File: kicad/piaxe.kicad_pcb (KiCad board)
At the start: 4 copper layers, 85 x 56 mm, 109 parts, among them J1 Barrel_Jack_Switch, J2 Conn_02x20_Odd_Even, J3 Conn_01x05, M1 Fan_4pin, Q1 CSD17576Q5B, Q2 CSD17308Q3, Q5 BSS138, Q6 BSS138, Q9 BSS138, U1 TPS40305, U13 TMP1075, U14 BM1366_mode1, U15 2N7001TDCK, U16 2N7001TDCK, U5 MCP1824T-1802E, U6 MCP1824T-0802E, U7 25MHz

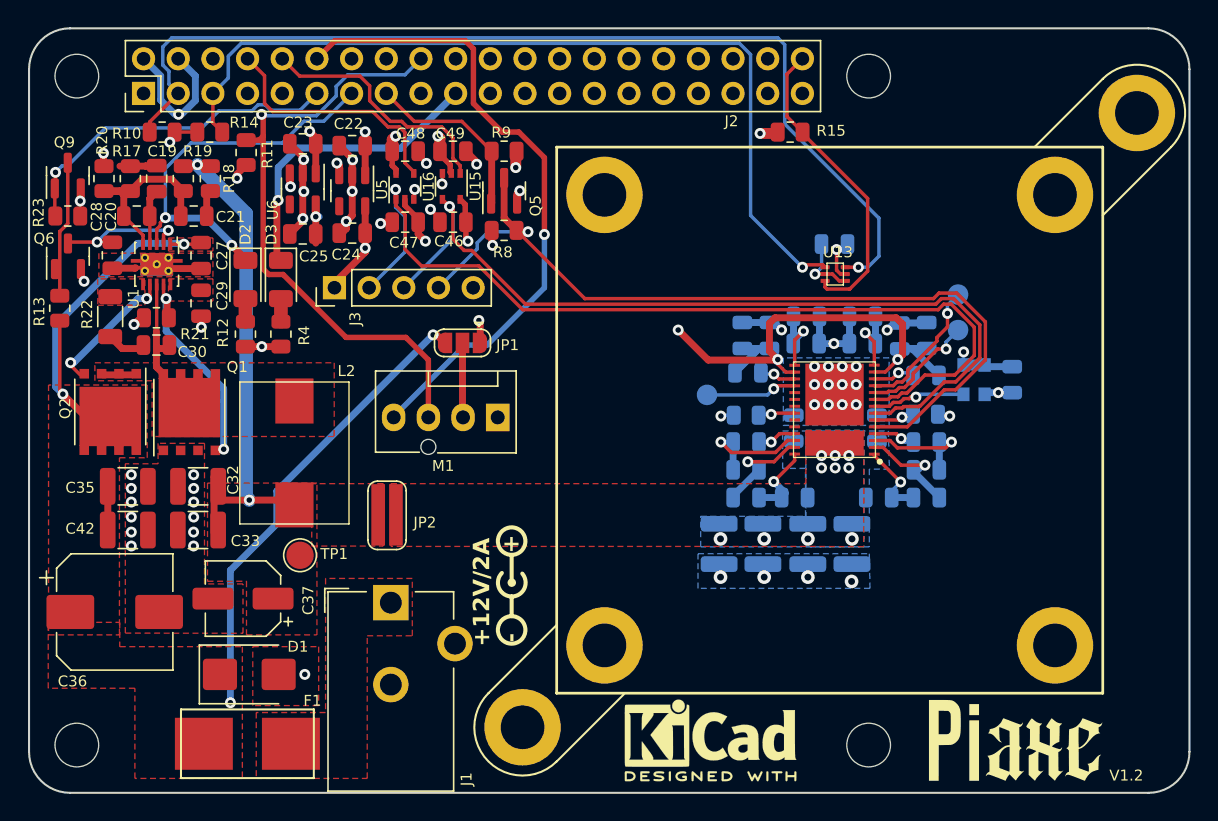
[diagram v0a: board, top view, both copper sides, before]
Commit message: added solderjumper to enable the buck without Pi, changed LED values to 560R
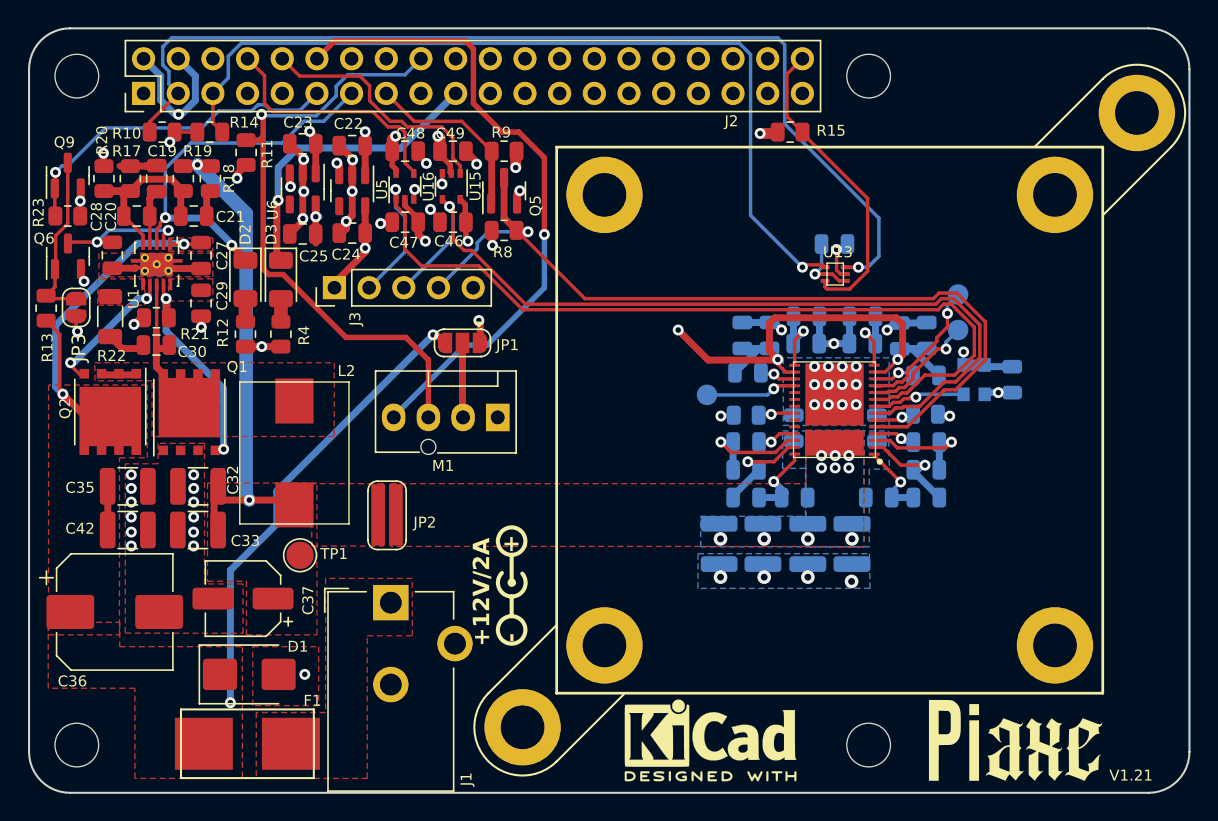
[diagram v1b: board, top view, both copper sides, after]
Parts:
- added JP3: SolderJumper_2_Open, Jumper:SolderJumper-2_P1.3mm_Open_RoundedPad1.0x1.5mm, F.Cu at (176.8, 76.2)
- R12, R4: value 1k -> 560
- moved R13 1.00 mm to (174.6, 76.3)
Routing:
- net Net-(JP3-A): track 10.1 -> 12.8 mm
- net GND: track 114.7 -> 115.9 mm, vias 57 -> 58
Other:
- board text added: "V1.21"
- board text removed: "V1.2"

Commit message: fixed net labeling to 1.2V
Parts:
- TP1: value +1V5 -> +1V2
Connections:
- net +1V5 renamed +1V2
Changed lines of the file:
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@@
   (net 5 "Net-(U14-VDD2_0)")
   (net 6 "Net-(U14-VDD1_0)")
-  (net 7 "+1V5")
+  (net 7 "+1V2")
   (net 8 "Net-(U14-VDD1_1)")
   (net 9 "Net-(U14-VDD2_1)")
@@
       ))
     (pad "2" smd custom (at 0.524 -0.234) (size 1 4.5) (layers "F.Cu" "F.Mask")
-      (net 7 "+1V5") (pinfunction "B") (pintype "passive") (zone_connect 2) (thermal_bridge_angle 45)
+      (net 7 "+1V2") (pinfunction "B") (pintype "passive") (zone_connect 2) (thermal_bridge_angle 45)
       (options (clearance outline) (anchor rect))
       (primitives
@@
         (effects (font (size 0.8 0.8) (thickness 0.15)))
     )
-    (fp_text value "+1V5" (at 0 2.05) (layer "F.Fab")
+    (fp_text value "+1V2" (at 0 2.05) (layer "F.Fab")
         (effects (font (size 1 1) (thickness 0.15)))
     )
@@
       (net 8 "Net-(U14-VDD1_1)") (pinfunction "VDD1_1") (pintype "input") (thermal_bridge_angle 45))
     (pad "29" smd rect locked (at 0 -2.468 180) (size 4.277 1.81) (layers "F.Cu" "F.Mask")
-      (net 7 "+1V5") (pinfunction "VDD") (pintype "input") (thermal_bridge_angle 45))
+      (net 7 "+1V2") (pinfunction "VDD") (pintype "input") (thermal_bridge_angle 45))
     (pad "30" smd rect locked (at 0 1.108 180) (size 4.277 4.53) (layers "F.Cu" "F.Mask")
       (net 1 "GND") (pinfunction "GND") (pintype "input") (thermal_bridge_angle 45))
@@
       (stroke (width 0.1) (type solid)) (layer "B.Fab"))
     (pad "1" smd roundrect (at -0.95 0 90) (size 1 1.45) (layers "B.Cu" "B.Paste" "B.Mask") (roundrect_rratio 0.25)
-      (net 7 "+1V5") (pintype "passive"))
+      (net 7 "+1V2") (pintype "passive"))
     (pad "2" smd roundrect (at 0.95 0 90) (size 1 1.45) (layers "B.Cu" "B.Paste" "B.Mask") (roundrect_rratio 0.25)
       (net 1 "GND") (pintype "passive"))
@@
       (stroke (width 0.1) (type solid)) (layer "B.Fab"))
     (pad "1" smd roundrect (at -0.95 0 90) (size 1 1.45) (layers "B.Cu" "B.Paste" "B.Mask") (roundrect_rratio 0.25)
-      (net 7 "+1V5") (pintype "passive"))
+      (net 7 "+1V2") (pintype "passive"))
     (pad "2" smd roundrect (at 0.95 0 90) (size 1 1.45) (layers "B.Cu" "B.Paste" "B.Mask") (roundrect_rratio 0.25)
       (net 1 "GND") (pintype "passive"))
@@
       (stroke (width 0.1) (type solid)) (layer "B.Fab"))
     (pad "1" smd roundrect (at -1.475 0 270) (size 1.15 2.7) (layers "B.Cu" "B.Paste" "B.Mask") (roundrect_rratio 0.2173913043)
-      (net 7 "+1V5") (pintype "passive"))
+      (net 7 "+1V2") (pintype "passive"))
     (pad "2" smd roundrect (at 1.475 0 270) (size 1.15 2.7) (layers "B.Cu" "B.Paste" "B.Mask") (roundrect_rratio 0.2173913043)
       (net 1 "GND") (pintype "passive"))
@@
       (stroke (width 0.1) (type solid)) (layer "B.Fab"))
     (pad "1" smd roundrect (at -0.95 0 180) (size 1 1.45) (layers "B.Cu" "B.Paste" "B.Mask") (roundrect_rratio 0.25)
-      (net 7 "+1V5") (pintype "passive"))
+      (net 7 "+1V2") (pintype "passive"))
     (pad "2" smd roundrect (at 0.95 0 180) (size 1 1.45) (layers "B.Cu" "B.Paste" "B.Mask") (roundrect_rratio 0.25)
       (net 8 "Net-(U14-VDD1_1)") (pintype "passive"))
@@
       (stroke (width 0.1) (type solid)) (layer "B.Fab"))
     (pad "1" smd roundrect (at -1.475 0 270) (size 1.15 2.7) (layers "B.Cu" "B.Paste" "B.Mask") (roundrect_rratio 0.2173913043)
-      (net 7 "+1V5") (pintype "passive"))
+      (net 7 "+1V2") (pintype "passive"))
     (pad "2" smd roundrect (at 1.475 0 270) (size 1.15 2.7) (layers "B.Cu" "B.Paste" "B.Mask") (roundrect_rratio 0.2173913043)
       (net 1 "GND") (pintype "passive"))
@@
       (stroke (width 0.1) (type solid)) (layer "B.Fab"))
     (pad "1" smd roundrect (at -0.95 0 90) (size 1 1.45) (layers "B.Cu" "B.Paste" "B.Mask") (roundrect_rratio 0.25)
-      (net 7 "+1V5") (pintype "passive"))
+      (net 7 "+1V2") (pintype "passive"))
     (pad "2" smd roundrect (at 0.95 0 90) (size 1 1.45) (layers "B.Cu" "B.Paste" "B.Mask") (roundrect_rratio 0.25)
       (net 1 "GND") (pintype "passive"))
@@
       (stroke (width 0.1) (type solid)) (layer "B.Fab"))
     (pad "1" smd roundrect (at -1.475 0 270) (size 1.15 2.7) (layers "B.Cu" "B.Paste" "B.Mask") (roundrect_rratio 0.2173913043)
-      (net 7 "+1V5") (pintype "passive"))
+      (net 7 "+1V2") (pintype "passive"))
     (pad "2" smd roundrect (at 1.475 0 270) (size 1.15 2.7) (layers "B.Cu" "B.Paste" "B.Mask") (roundrect_rratio 0.2173913043)
       (net 1 "GND") (pintype "passive"))
@@
       (stroke (width 0.1) (type solid)) (layer "B.Fab"))
     (pad "1" smd roundrect (at -0.95 0 90) (size 1 1.45) (layers "B.Cu" "B.Paste" "B.Mask") (roundrect_rratio 0.25)
-      (net 7 "+1V5") (pintype "passive"))
+      (net 7 "+1V2") (pintype "passive"))
     (pad "2" smd roundrect (at 0.95 0 90) (size 1 1.45) (layers "B.Cu" "B.Paste" "B.Mask") (roundrect_rratio 0.25)
       (net 1 "GND") (pintype "passive"))
@@
       (stroke (width 0.1) (type solid)) (layer "B.Fab"))
     (pad "1" smd roundrect (at -1.475 0 270) (size 1.15 2.7) (layers "B.Cu" "B.Paste" "B.Mask") (roundrect_rratio 0.2173913043)
-      (net 7 "+1V5") (pintype "passive"))
+      (net 7 "+1V2") (pintype "passive"))
     (pad "2" smd roundrect (at 1.475 0 270) (size 1.15 2.7) (layers "B.Cu" "B.Paste" "B.Mask") (roundrect_rratio 0.2173913043)
       (net 1 "GND") (pintype "passive"))
@@
       (net 6 "Net-(U14-VDD1_0)") (pintype "passive"))
     (pad "2" smd roundrect (at 0.95 0 180) (size 1 1.45) (layers "B.Cu" "B.Paste" "B.Mask") (roundrect_rratio 0.25)
-      (net 7 "+1V5") (pintype "passive"))
+      (net 7 "+1V2") (pintype "passive"))
     (model "${KICAD6_3DMODEL_DIR}/Capacitor_SMD.3dshapes/C_0805_2012Metric.wrl"
       (offset (xyz 0 0 0))
@@
     )
   )
-  (zone (net 7) (net_name "+1V5") (layer "F.Cu") (hatch edge 0.5)
+  (zone (net 7) (net_name "+1V2") (layer "F.Cu") (hatch edge 0.5)
     (priority 9)
     (connect_pads yes (clearance 0.4))
@@
     )
   )
-  (zone (net 7) (net_name "+1V5") (layer "B.Cu") (hatch edge 0.5)
+  (zone (net 7) (net_name "+1V2") (layer "B.Cu") (hatch edge 0.5)
     (priority 10)
     (connect_pads yes (clearance 0.4))
@@
     )
   )
-  (zone (net 7) (net_name "+1V5") (layer "B.Cu") (hatch edge 0.5)
+  (zone (net 7) (net_name "+1V2") (layer "B.Cu") (hatch edge 0.5)
     (priority 13)
     (connect_pads yes (clearance 0.4))

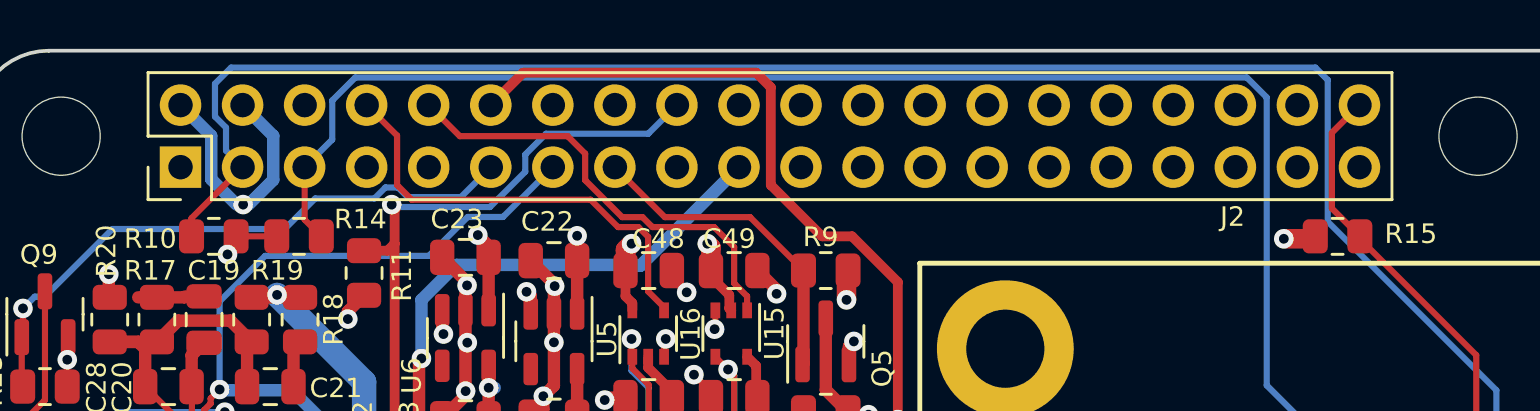
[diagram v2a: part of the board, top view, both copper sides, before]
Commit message: switched pinheader on top to pinsocket on bottom
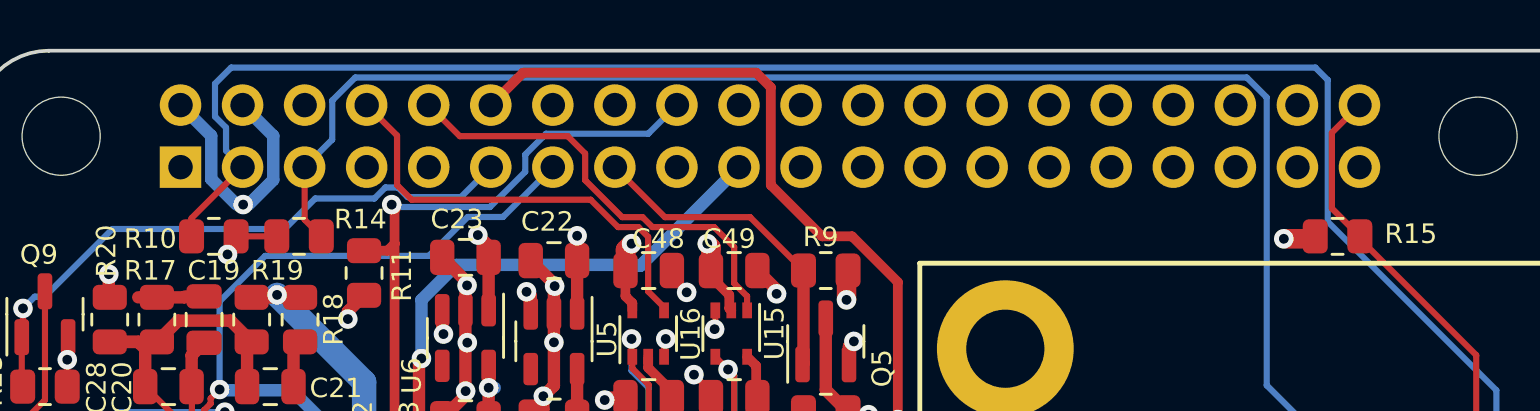
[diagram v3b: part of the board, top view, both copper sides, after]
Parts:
- J2: footprint Connector_PinHeader_2.54mm:PinHeader_2x20_P2.54mm_Vertical -> Connector_PinSocket_2.54mm:PinSocket_2x20_P2.54mm_Vertical; moved to B.Cu
- Q2: value CSD17308Q3 -> CSD17576Q5B
- turned J2 to -90 degrees
